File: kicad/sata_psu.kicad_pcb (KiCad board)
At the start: 2 copper layers, 64.2 x 53.3 mm, 56 parts, among them J1 12V/GND/GND/5V, J2 12V/GND/GND/5V, J3 12V/GND/GND/5V, J4 12V/GND/GND/5V, J5 12V/GND/GND/5V, J8 12V DC 8-10A, Q1 AO3401A, Q2 AO3401A, Q3 AO3401A, Q4 AO3401A, Q5 AO3401A, Q8 AOD4185, U9 TPS563200

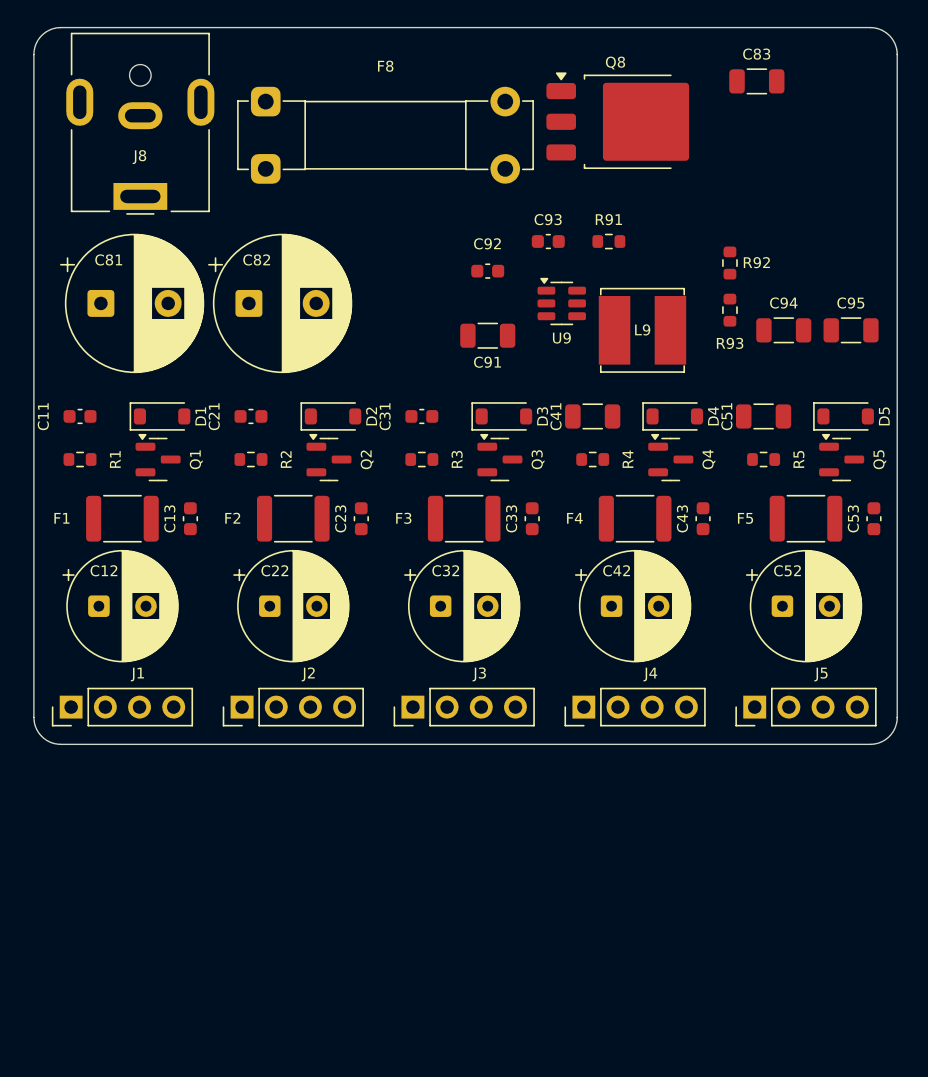
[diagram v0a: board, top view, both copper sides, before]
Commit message: v2: per-port 5V buck with 0R neighbour sharing, plus rail indicators
Every port now has its own local 5V node and its own buck footprint, with
adjacent nodes joined by 0R links (R61-R64). How a port gets its 5V is a
populate choice rather than a layout one -- BUCKS/LINKS at the top of
gen_sch.py is the whole configuration, and the lands are always present.

This closes v1's largest open issue. One 3A TPS563200 was under-rated
against a five-bay 5V rail; capping a buck at a three-port group makes its
worst case 2.1A and the same part is correctly sized.

Indicators: one 12V LED on the common rail, tapped after Q8 so it also
proves the reverse-polarity guard conducts, and one 5V LED per port on the
local node at the header, so it lights whether that port's 5V came from its
own buck or across a link.

verify.py gains check 5, the rail populate rules. A DNP part is still a
wire in the netlist, so a build that fits R63 with both U2 and U4 populated
passes ERC and netlist equivalence and parallels two regulators on the
bench. Nothing else can catch it. It also refuses groups over three ports
and any link carrying more than one port's current.

Also fixed: check_layout.py reported "0 symbols checked" and PASSED after
KiCad re-saved the sheets in its own format, because text[text.find(m):]
yields the last character rather than "" when the marker is absent, so the
`or text` fallback never fired. It now fails loudly when it parses nothing.

Schematic verified (ERC clean, 50 nets equivalent to the independent SKiDL
description, pins match pads). Board placed at 64.9 x 76.0 mm, 112 parts,
0 DRC violations. Routing still not started.

Co-Authored-By: Claude Opus 5 <noreply@anthropic.com>
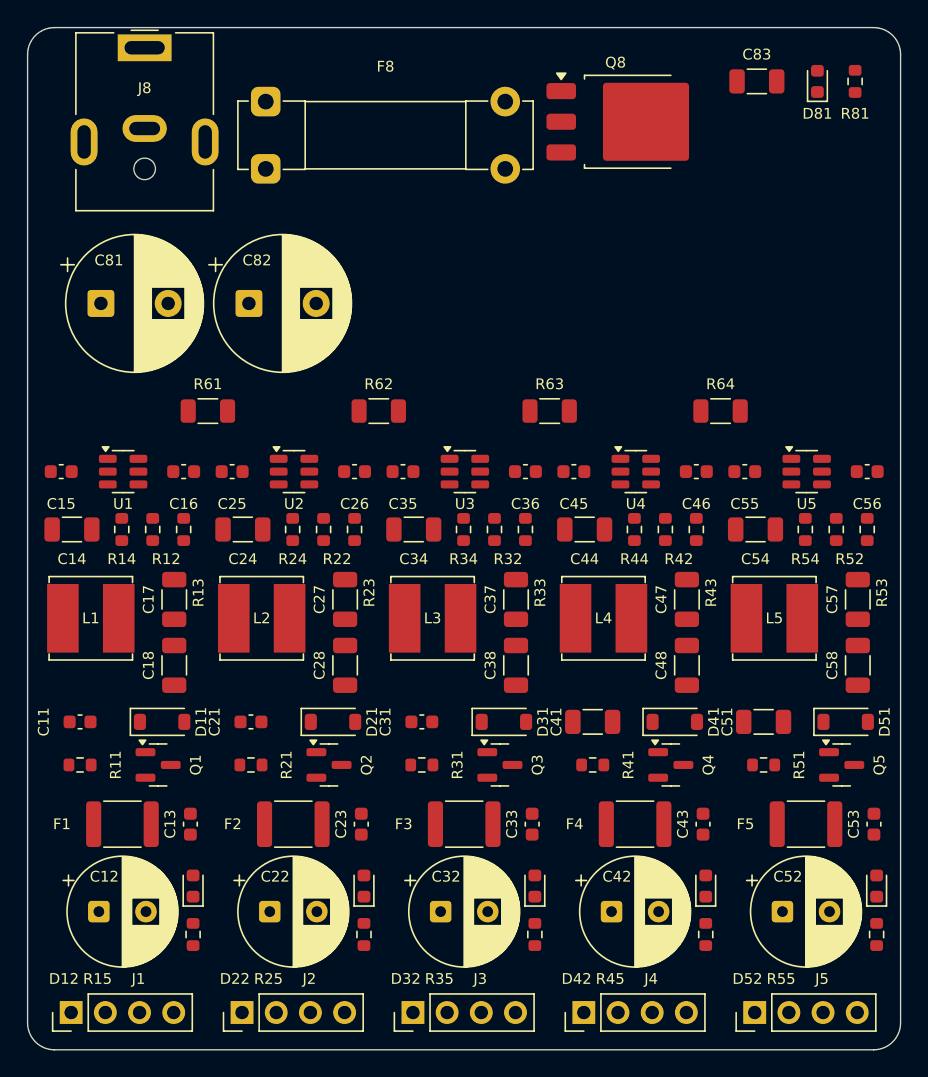
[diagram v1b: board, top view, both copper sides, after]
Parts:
- removed C91: 10uF/50V, Capacitor_SMD:C_1206_3216Metric
- removed C92, C93: 100nF, Capacitor_SMD:C_0603_1608Metric
- removed C94, C95: 22uF/25V, Capacitor_SMD:C_1206_3216Metric
- removed D1, D2, D3, D4, D5: 8.2V, Diode_SMD:D_SOD-123
- removed L9: 4.7uH/4.5A, Inductor_SMD:L_Bourns_SRN6045TA
- removed R1, R2, R3, R4, R5: 220k, Resistor_SMD:R_0603_1608Metric
- removed R91: 100k, Resistor_SMD:R_0603_1608Metric
- removed R92: 56k, Resistor_SMD:R_0603_1608Metric
- removed R93: 10k, Resistor_SMD:R_0603_1608Metric
- removed U9: TPS563200, Package_TO_SOT_SMD:SOT-23-6
- added C14: 10uF/50V, Capacitor_SMD:C_1206_3216Metric, F.Cu at (33.6, 67.3)
- added C15: 100nF, Capacitor_SMD:C_0603_1608Metric, F.Cu at (32.8, 63.0)
- added C16: 100nF, Capacitor_SMD:C_0603_1608Metric, F.Cu at (41.9, 63.0)
- added C17: 22uF/25V, Capacitor_SMD:C_1206_3216Metric, F.Cu at (41.2, 72.5)
- added C18: 22uF/25V, Capacitor_SMD:C_1206_3216Metric, F.Cu at (41.2, 77.4)
- added C24: 10uF/50V, Capacitor_SMD:C_1206_3216Metric, F.Cu at (46.3, 67.3)
- added C25: 100nF, Capacitor_SMD:C_0603_1608Metric, F.Cu at (45.5, 63.0)
- added C26: 100nF, Capacitor_SMD:C_0603_1608Metric, F.Cu at (54.6, 63.0)
- added C27: 22uF/25V, Capacitor_SMD:C_1206_3216Metric, F.Cu at (53.9, 72.5)
- added C28: 22uF/25V, Capacitor_SMD:C_1206_3216Metric, F.Cu at (53.9, 77.4)
- added C34: 10uF/50V, Capacitor_SMD:C_1206_3216Metric, F.Cu at (59.0, 67.3)
- added C35: 100nF, Capacitor_SMD:C_0603_1608Metric, F.Cu at (58.2, 63.0)
- added C36: 100nF, Capacitor_SMD:C_0603_1608Metric, F.Cu at (67.3, 63.0)
- added C37: 22uF/25V, Capacitor_SMD:C_1206_3216Metric, F.Cu at (66.6, 72.5)
- added C38: 22uF/25V, Capacitor_SMD:C_1206_3216Metric, F.Cu at (66.6, 77.4)
- added C44: 10uF/50V, Capacitor_SMD:C_1206_3216Metric, F.Cu at (71.7, 67.3)
- added C45: 100nF, Capacitor_SMD:C_0603_1608Metric, F.Cu at (70.9, 63.0)
- added C46: 100nF, Capacitor_SMD:C_0603_1608Metric, F.Cu at (80.0, 63.0)
- added C47: 22uF/25V, Capacitor_SMD:C_1206_3216Metric, F.Cu at (79.3, 72.5)
- added C48: 22uF/25V, Capacitor_SMD:C_1206_3216Metric, F.Cu at (79.3, 77.4)
- added C54: 10uF/50V, Capacitor_SMD:C_1206_3216Metric, F.Cu at (84.4, 67.3)
- added C55: 100nF, Capacitor_SMD:C_0603_1608Metric, F.Cu at (83.6, 63.0)
- added C56: 100nF, Capacitor_SMD:C_0603_1608Metric, F.Cu at (92.7, 63.0)
- added C57: 22uF/25V, Capacitor_SMD:C_1206_3216Metric, F.Cu at (92.0, 72.5)
- added C58: 22uF/25V, Capacitor_SMD:C_1206_3216Metric, F.Cu at (92.0, 77.4)
- added D11: 8.2V, Diode_SMD:D_SOD-123, F.Cu at (40.3, 81.6)
- added D12: GRN, LED_SMD:LED_0603_1608Metric, F.Cu at (42.6, 93.8)
- added D21: 8.2V, Diode_SMD:D_SOD-123, F.Cu at (53.0, 81.6)
- added D22: GRN, LED_SMD:LED_0603_1608Metric, F.Cu at (55.3, 93.8)
- added D31: 8.2V, Diode_SMD:D_SOD-123, F.Cu at (65.7, 81.6)
- added D32: GRN, LED_SMD:LED_0603_1608Metric, F.Cu at (68.0, 93.8)
- added D41: 8.2V, Diode_SMD:D_SOD-123, F.Cu at (78.4, 81.6)
- added D42: GRN, LED_SMD:LED_0603_1608Metric, F.Cu at (80.7, 93.8)
- added D51: 8.2V, Diode_SMD:D_SOD-123, F.Cu at (91.1, 81.6)
- added D52: GRN, LED_SMD:LED_0603_1608Metric, F.Cu at (93.4, 93.8)
- added D81: GRN, LED_SMD:LED_0603_1608Metric, F.Cu at (89.0, 34.0)
- added L1: 4.7uH/4.5A, Inductor_SMD:L_Bourns_SRN6045TA, F.Cu at (35.0, 73.9)
- added L2: 4.7uH/4.5A, Inductor_SMD:L_Bourns_SRN6045TA, F.Cu at (47.7, 73.9)
- added L3: 4.7uH/4.5A, Inductor_SMD:L_Bourns_SRN6045TA, F.Cu at (60.4, 73.9)
- added L4: 4.7uH/4.5A, Inductor_SMD:L_Bourns_SRN6045TA, F.Cu at (73.1, 73.9)
- added L5: 4.7uH/4.5A, Inductor_SMD:L_Bourns_SRN6045TA, F.Cu at (85.8, 73.9)
- added R11: 220k, Resistor_SMD:R_0603_1608Metric, F.Cu at (34.2, 84.8)
- added R12: 56k, Resistor_SMD:R_0603_1608Metric, F.Cu at (39.6, 67.3)
- added R13: 10k, Resistor_SMD:R_0603_1608Metric, F.Cu at (41.9, 67.3)
- added R14: 100k, Resistor_SMD:R_0603_1608Metric, F.Cu at (37.3, 67.3)
- added R15: 1.5k, Resistor_SMD:R_0603_1608Metric, F.Cu at (42.6, 97.4)
- added R21: 220k, Resistor_SMD:R_0603_1608Metric, F.Cu at (46.9, 84.8)
- added R22: 56k, Resistor_SMD:R_0603_1608Metric, F.Cu at (52.3, 67.3)
- added R23: 10k, Resistor_SMD:R_0603_1608Metric, F.Cu at (54.6, 67.3)
- added R24: 100k, Resistor_SMD:R_0603_1608Metric, F.Cu at (50.0, 67.3)
- added R25: 1.5k, Resistor_SMD:R_0603_1608Metric, F.Cu at (55.3, 97.4)
- added R31: 220k, Resistor_SMD:R_0603_1608Metric, F.Cu at (59.6, 84.8)
- added R32: 56k, Resistor_SMD:R_0603_1608Metric, F.Cu at (65.0, 67.3)
- added R33: 10k, Resistor_SMD:R_0603_1608Metric, F.Cu at (67.3, 67.3)
- added R34: 100k, Resistor_SMD:R_0603_1608Metric, F.Cu at (62.7, 67.3)
- added R35: 1.5k, Resistor_SMD:R_0603_1608Metric, F.Cu at (68.0, 97.4)
- added R41: 220k, Resistor_SMD:R_0603_1608Metric, F.Cu at (72.3, 84.8)
- added R42: 56k, Resistor_SMD:R_0603_1608Metric, F.Cu at (77.7, 67.3)
- added R43: 10k, Resistor_SMD:R_0603_1608Metric, F.Cu at (80.0, 67.3)
- added R44: 100k, Resistor_SMD:R_0603_1608Metric, F.Cu at (75.4, 67.3)
- added R45: 1.5k, Resistor_SMD:R_0603_1608Metric, F.Cu at (80.7, 97.4)
- added R51: 220k, Resistor_SMD:R_0603_1608Metric, F.Cu at (85.0, 84.8)
- added R52: 56k, Resistor_SMD:R_0603_1608Metric, F.Cu at (90.4, 67.3)
- added R53: 10k, Resistor_SMD:R_0603_1608Metric, F.Cu at (92.7, 67.3)
- added R54: 100k, Resistor_SMD:R_0603_1608Metric, F.Cu at (88.1, 67.3)
- added R55: 1.5k, Resistor_SMD:R_0603_1608Metric, F.Cu at (93.4, 97.4)
- added R61: 0R, Resistor_SMD:R_1206_3216Metric, F.Cu at (43.7, 58.5)
- added R62: 0R, Resistor_SMD:R_1206_3216Metric, F.Cu at (56.4, 58.5)
- added R63: 0R, Resistor_SMD:R_1206_3216Metric, F.Cu at (69.1, 58.5)
- added R64: 0R, Resistor_SMD:R_1206_3216Metric, F.Cu at (81.8, 58.5)
- added R81: 4.7k, Resistor_SMD:R_0603_1608Metric, F.Cu at (91.8, 34.0)
- added U1: TPS563200, Package_TO_SOT_SMD:SOT-23-6, F.Cu at (37.4, 63.0)
- added U2: TPS563200, Package_TO_SOT_SMD:SOT-23-6, F.Cu at (50.1, 63.0)
- added U3: TPS563200, Package_TO_SOT_SMD:SOT-23-6, F.Cu at (62.8, 63.0)
- added U4: TPS563200, Package_TO_SOT_SMD:SOT-23-6, F.Cu at (75.5, 63.0)
- added U5: TPS563200, Package_TO_SOT_SMD:SOT-23-6, F.Cu at (88.2, 63.0)
- moved C12 22.7 mm to (35.6, 95.7)
- moved C13 22.7 mm to (42.4, 89.2)
- moved C22 22.7 mm to (48.3, 95.7)
- moved C23 22.7 mm to (55.1, 89.2)
- moved C32 22.7 mm to (61.0, 95.7)
- moved C33 22.7 mm to (67.8, 89.2)
- moved C42 22.7 mm to (73.7, 95.7)
- moved C43 22.7 mm to (80.5, 89.2)
- moved C52 22.7 mm to (86.4, 95.7)
- moved C53 22.7 mm to (93.2, 89.2)
- moved F1 22.7 mm to (37.4, 89.2)
- moved F2 22.7 mm to (50.0, 89.2)
- moved F3 22.7 mm to (62.8, 89.2)
- moved F4 22.7 mm to (75.5, 89.2)
- moved F5 22.7 mm to (88.2, 89.2)
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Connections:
- J1 pad 4: 5V_MAIN -> 5V_1
- J2 pad 4: 5V_MAIN -> 5V_2
- J3 pad 4: 5V_MAIN -> 5V_3
- J4 pad 4: 5V_MAIN -> 5V_4
- J5 pad 4: 5V_MAIN -> 5V_5
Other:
- board size 64.2 x 53.3 mm -> 64.9 x 76 mm

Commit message: v3: JLCPCB-ready layout, fab outputs and DigiKey BOM
Board (DRC clean against JLCPCB standard 2-layer rules, 0 errors,
0 unconnected, schematic parity clean):
- design rules set to JLCPCB limits; extra pad rules in sata_psu.kicad_dru
- buck GND pins (U1-U5) were on isolated F.Cu islands: stitched to B.Cu
- C41/C51 1206 pads restored from 0603 pitch to library land pattern
- replicated SW via patches re-netted (ch2/4/5), missing ones added
- duplicate 12V zone and dangling vias on ch1 removed; 0.4 vias -> 0.45
- gate-cap courtyards in ch4/ch5 cleared; DNP flags synced from schematic
- refdes resized to 1.0/0.15 mm and placed clear of pads and silk

Outputs: Gerbers + Excellon drill (gerbers/, sata_psu_jlcpcb.zip) and
DigiKey BOM with in-stock substitutes plus a cart upload CSV.

Co-Authored-By: Claude Opus 5.5 <noreply@anthropic.com>
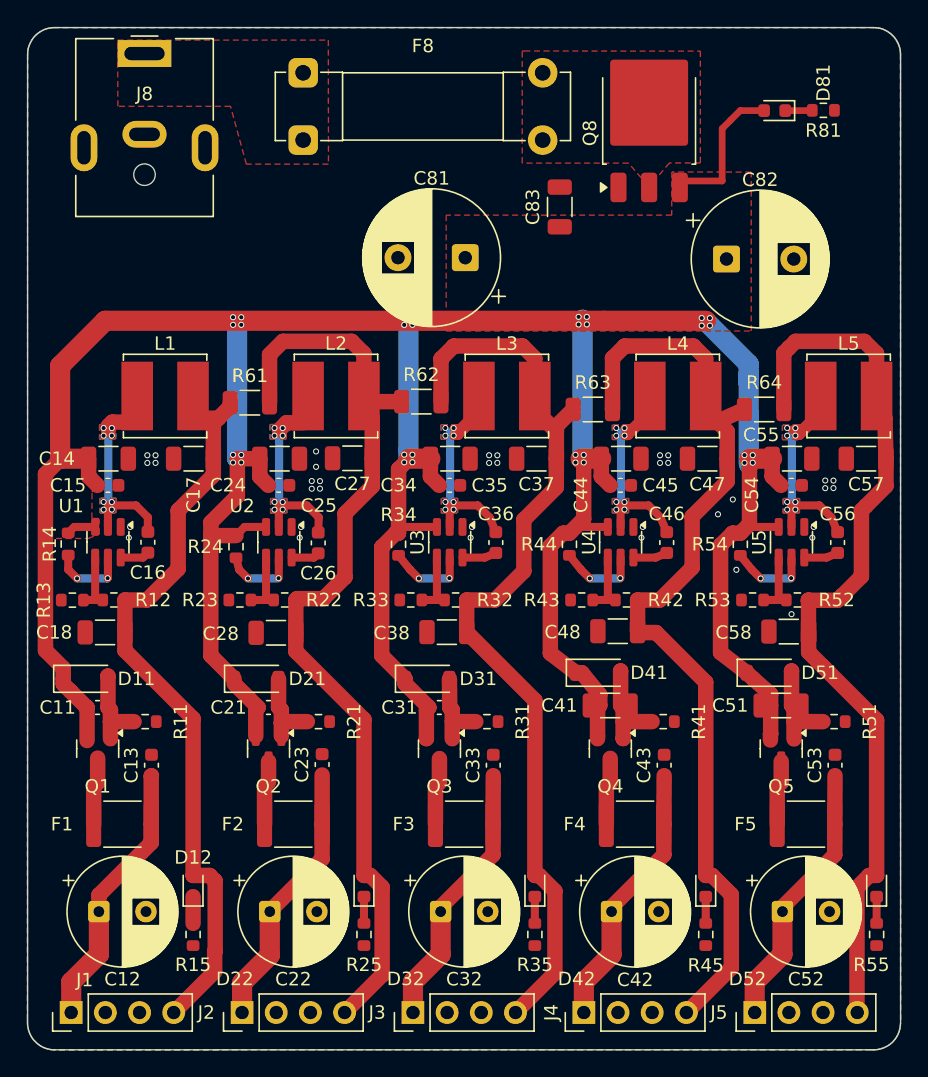
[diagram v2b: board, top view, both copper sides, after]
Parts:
- moved C82 35.6 mm to (82.2, 47.2)
- moved C81 27.3 mm to (62.8, 47.1), turned to 180 degrees
- moved L1 17.4 mm to (40.5, 57.4)
- moved L3 17.4 mm to (65.9, 57.4)
- moved L4 17.4 mm to (78.6, 57.4)
- moved L2 17.4 mm to (53.2, 57.4)
- moved L5 17.4 mm to (91.3, 57.4)
- moved C83 17.4 mm to (69.8, 43.3), turned to 90 degrees
- moved C37 10.6 mm to (68.1, 62.0), turned to 180 degrees
- moved C47 10.6 mm to (80.8, 62.0), turned to 180 degrees
- moved C17 10.6 mm to (42.6, 62.0), turned to 180 degrees
- moved C27 10.5 mm to (54.4, 62.0), turned to 180 degrees
- moved C57 10.5 mm to (92.6, 62.0), turned to 180 degrees
- moved R23 10.0 mm to (46.1, 72.5), turned to 180 degrees
- moved R33 10.0 mm to (58.8, 72.5), turned to 180 degrees
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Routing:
- net 12V_MAIN: track 0.00 -> 261.8 mm, vias 0 -> 32
- net 5V_4: track 0.00 -> 71.4 mm
- net 5V_2: track 0.00 -> 71.0 mm
- net 5V_3: track 0.00 -> 70.4 mm
- net 5V_5: track 0.00 -> 68.5 mm
- net 5V_1: track 0.00 -> 57.6 mm
- net Net-(J2-Pin_1): track 0.00 -> 20.1 mm
- net Net-(J1-Pin_1): track 0.00 -> 20.1 mm
- net Net-(J3-Pin_1): track 0.00 -> 20.1 mm
- net Net-(J5-Pin_1): track 0.00 -> 20.1 mm
- net Net-(J4-Pin_1): track 0.00 -> 20.1 mm
- net Net-(U3-SW): track 0.00 -> 17.0 mm, vias 0 -> 8
- net Net-(U4-SW): track 0.00 -> 16.8 mm, vias 0 -> 8
- net Net-(U1-SW): track 0.00 -> 16.7 mm, vias 0 -> 8
- net Net-(U5-SW): track 0.00 -> 16.4 mm, vias 0 -> 8
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- added copper zone on F.Cu, net 12V_MAIN
- added copper zone on B.Cu, net GND
- added copper zone on F.Cu, net GND
- added copper zone on F.Cu, net Net-(F8-Pad1)
- added copper zone on F.Cu, net Net-(Q8-D)
- added copper zone on B.Cu, net Net-(U1-SW)
- added copper zone on F.Cu, net Net-(U1-SW)
- added copper zone on B.Cu, net Net-(U2-SW)
- added copper zone on F.Cu, net Net-(U2-SW)
- added copper zone on B.Cu, net Net-(U3-SW)
- added copper zone on F.Cu, net Net-(U3-SW)
- added copper zone on B.Cu, net Net-(U4-SW)
- added copper zone on F.Cu, net Net-(U4-SW)
- added copper zone on B.Cu, net Net-(U5-SW)
- added copper zone on F.Cu, net Net-(U5-SW)
